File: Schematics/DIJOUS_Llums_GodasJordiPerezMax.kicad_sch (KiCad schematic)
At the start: 95 parts, among them J1 Conn_01x05_Socket, J10 Screw_Terminal_01x02, J11 Conn_01x06, J5 Conn_01x05, J6 Conn_01x03, J7 Conn_01x02, J8 DE9_Plug, J9 Conn_01x06_Socket, K1 G5LE-1 DC12, K3 G5LE-1 DC12, Q1 ZXTN19020DFFTA, Q10 ZXTN19020DFFTA, Q3 Si7336ADP, Q4 Si7336ADP, Q5 ZXTN19020DFFTA, Q6 ZXTN19020DFFTA, Q7 Si7336ADP, Q8 Si7336ADP, Q9 ZXTN19020DFFTA, U1 LT6202CS5, U2 LM2596T-ADJ, U3 PIC18F2580-I/SO, U4 MCP2551-I-SN, U5 ADP7112ACBZ-3.3-R7, U6 ADM7172ACPZ-5.0-R7, U7 PCA9306D, k2 1k

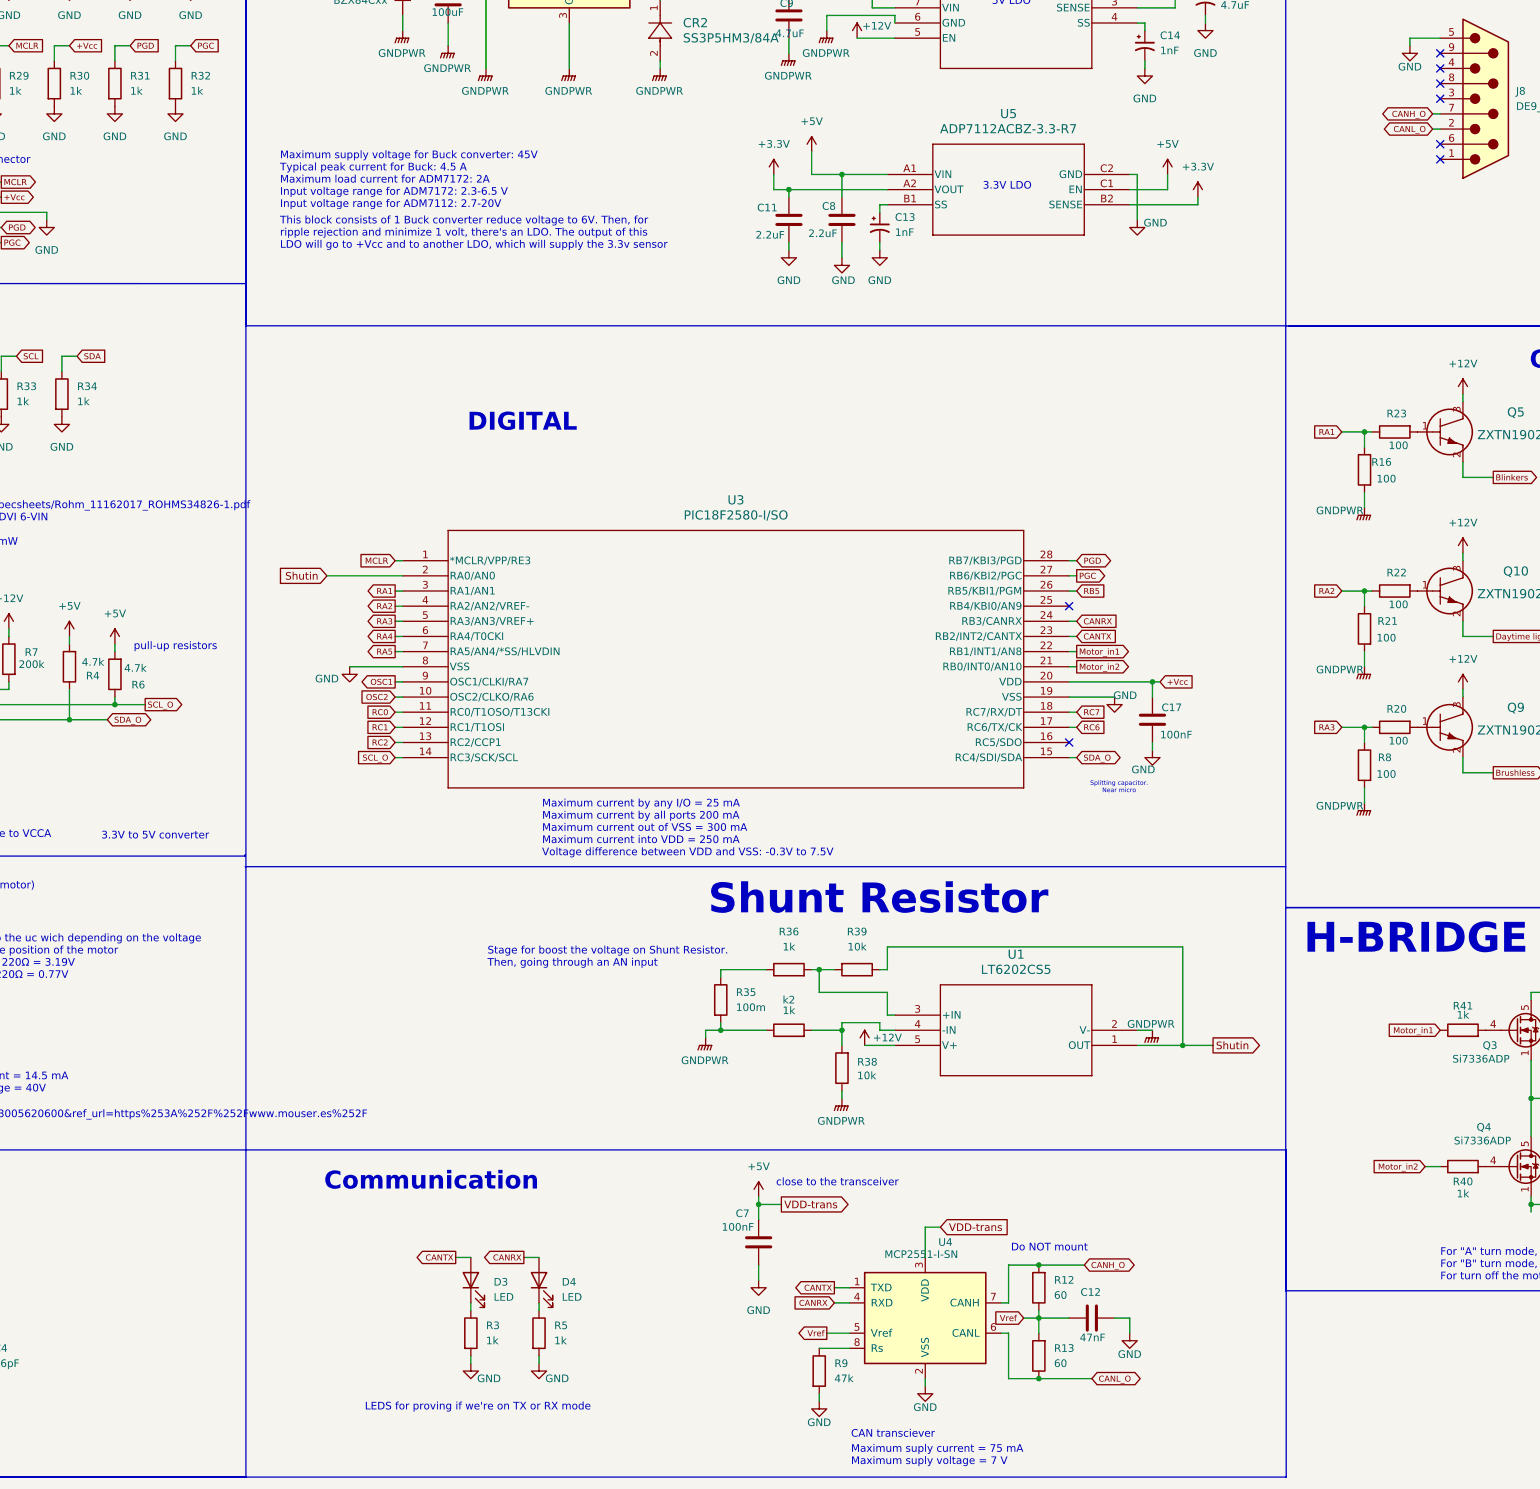
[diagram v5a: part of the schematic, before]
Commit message: Update DIJOUS_Llums_GodasJordiPerezMax.kicad_sch
Se ha cambiado alguna etiqueta
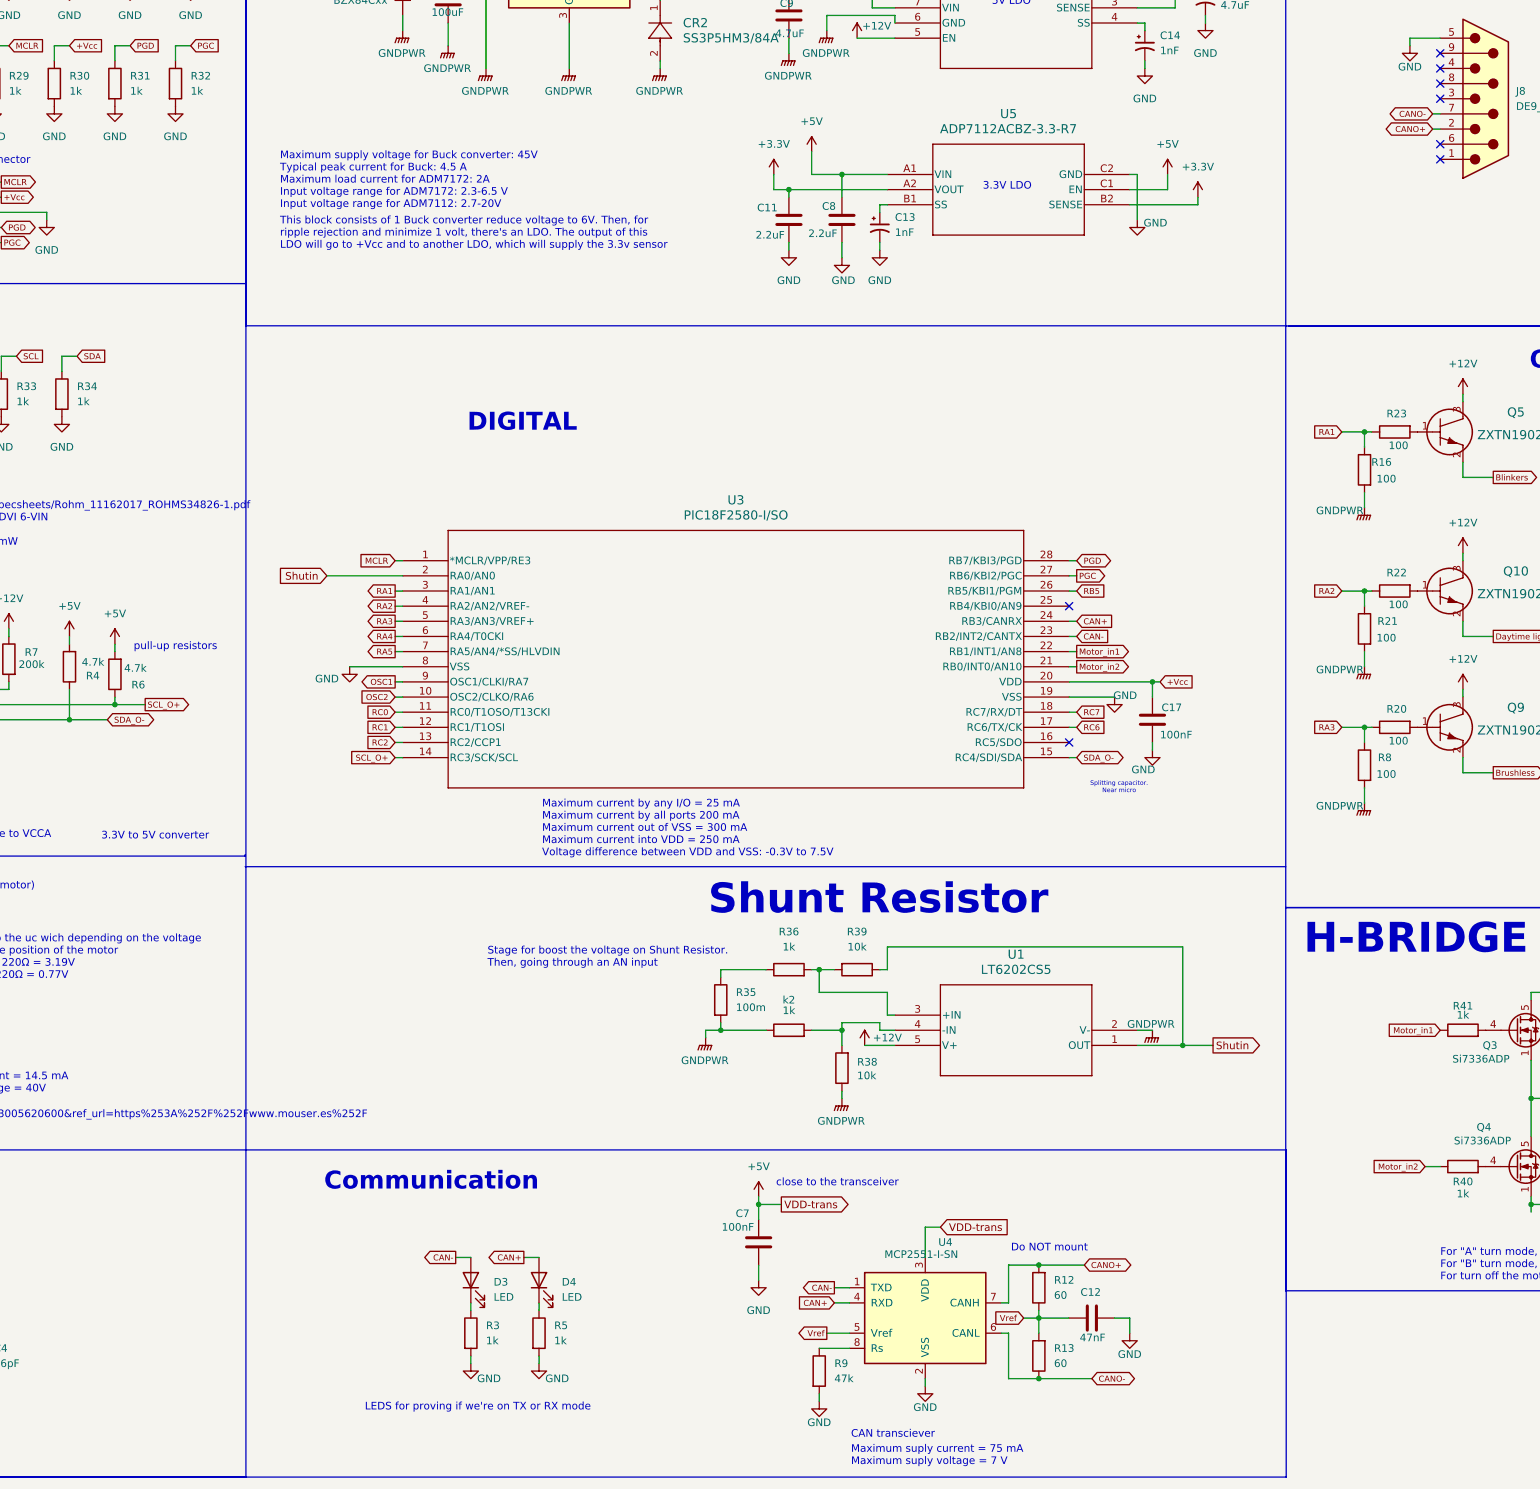
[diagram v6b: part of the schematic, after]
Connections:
- net CANH_O renamed CANO+
- net CANO+: now also J8.2; no longer J8.7
- net CANL_O renamed CANO-
- net CANO-: now also J8.7; no longer J8.2
- net CANRX renamed CAN+
- net CANTX renamed CAN-
- net SCL_O renamed SCL_O+
- net SDA_O renamed SDA_O-
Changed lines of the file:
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@@
 		)
 	)
-	(global_label "CANH_O"
+	(global_label "CANO-"
 		(shape bidirectional)
 		(at 316.23 55.88 180)
@@
 		)
 		(property "Intersheetrefs" "${INTERSHEET_REFS}"
-			(at 307.4929 55.88 0)
+			(at 307.8143 55.88 0)
 			(effects
 				(font
@@
 		)
 	)
-	(global_label "CANRX"
+	(global_label "CAN+"
 		(shape output)
 		(at 163.83 247.65 180)
@@
 		)
 		(property "Intersheetrefs" "${INTERSHEET_REFS}"
-			(at 156.6226 247.65 0)
-			(effects
-				(font
-					(size 1.27 1.27)
-				)
-				(justify right)
-				(hide yes)
-			)
-		)
-	)
-	(global_label "CANTX"
+			(at 157.3369 247.65 0)
+			(effects
+				(font
+					(size 1.27 1.27)
+				)
+				(justify right)
+				(hide yes)
+			)
+		)
+	)
+	(global_label "CAN-"
 		(shape output)
 		(at 152.4 247.65 180)
@@
 		)
 		(property "Intersheetrefs" "${INTERSHEET_REFS}"
-			(at 144.8057 247.65 0)
+			(at 145.9069 247.65 0)
 			(effects
 				(font
@@
 		)
 	)
-	(global_label "CANL_O"
+	(global_label "CANO-"
 		(shape bidirectional)
 		(at 259.08 267.97 0)
@@
 		)
 		(property "Intersheetrefs" "${INTERSHEET_REFS}"
-			(at 267.579 267.97 0)
+			(at 267.4957 267.97 0)
 			(effects
 				(font
@@
 		)
 	)
-	(global_label "CANL_O"
+	(global_label "CANO+"
 		(shape bidirectional)
 		(at 316.23 58.42 180)
@@
 		)
 		(property "Intersheetrefs" "${INTERSHEET_REFS}"
-			(at 307.731 58.42 0)
+			(at 307.8143 58.42 0)
 			(effects
 				(font
@@
 		)
 	)
-	(global_label "SDA_O"
+	(global_label "SDA_O-"
 		(shape bidirectional)
 		(at 93.98 157.48 0)
@@
 		)
 		(property "Intersheetrefs" "${INTERSHEET_REFS}"
-			(at 101.8243 157.48 0)
-			(effects
-				(font
-					(size 1.27 1.27)
-				)
-				(justify left)
-				(hide yes)
-			)
-		)
-	)
-	(global_label "CANH_O"
+			(at 103.0624 157.48 0)
+			(effects
+				(font
+					(size 1.27 1.27)
+				)
+				(justify left)
+				(hide yes)
+			)
+		)
+	)
+	(global_label "CANO+"
 		(shape bidirectional)
 		(at 257.81 248.92 0)
@@
 		)
 		(property "Intersheetrefs" "${INTERSHEET_REFS}"
-			(at 266.5471 248.92 0)
-			(effects
-				(font
-					(size 1.27 1.27)
-				)
-				(justify left)
-				(hide yes)
-			)
-		)
-	)
-	(global_label "CANRX"
+			(at 266.2257 248.92 0)
+			(effects
+				(font
+					(size 1.27 1.27)
+				)
+				(justify left)
+				(hide yes)
+			)
+		)
+	)
+	(global_label "CAN+"
 		(shape input)
 		(at 256.54 140.97 0)
@@
 		)
 		(property "Intersheetrefs" "${INTERSHEET_REFS}"
-			(at 263.7474 140.97 0)
+			(at 263.0331 140.97 0)
 			(effects
 				(font
@@
 		)
 	)
-	(global_label "SDA_O"
+	(global_label "SDA_O-"
 		(shape bidirectional)
 		(at 256.54 163.83 0)
@@
 		)
 		(property "Intersheetrefs" "${INTERSHEET_REFS}"
-			(at 263.5093 163.83 0)
+			(at 265.6224 163.83 0)
 			(effects
 				(font
@@
 		)
 	)
-	(global_label "SCL_O"
+	(global_label "SCL_O+"
 		(shape input)
 		(at 142.24 163.83 180)
@@
 		)
 		(property "Intersheetrefs" "${INTERSHEET_REFS}"
-			(at 135.3183 163.83 0)
+			(at 134.0802 163.83 0)
 			(effects
 				(font
@@
 		)
 	)
-	(global_label "SCL_O"
+	(global_label "SCL_O+"
 		(shape output)
 		(at 100.33 154.94 0)
@@
 		)
 		(property "Intersheetrefs" "${INTERSHEET_REFS}"
-			(at 107.2517 154.94 0)
+			(at 108.4898 154.94 0)
 			(effects
 				(font
@@
 		)
 	)
-	(global_label "CANTX"
+	(global_label "CAN-"
 		(shape input)
 		(at 256.54 143.51 0)
@@
 		)
 		(property "Intersheetrefs" "${INTERSHEET_REFS}"
-			(at 263.5093 143.51 0)
+			(at 263.0331 143.51 0)
 			(effects
 				(font
@@
 		)
 	)
-	(global_label "CANTX"
+	(global_label "CAN-"
 		(shape output)
 		(at 215.9 252.73 180)
@@
 		)
 		(property "Intersheetrefs" "${INTERSHEET_REFS}"
-			(at 208.3057 252.73 0)
+			(at 209.4069 252.73 0)
 			(effects
 				(font
@@
 		)
 	)
-	(global_label "CANRX"
+	(global_label "CAN+"
 		(shape input)
 		(at 215.9 255.27 180)
@@
 		)
 		(property "Intersheetrefs" "${INTERSHEET_REFS}"
-			(at 208.0676 255.27 0)
-			(effects
-				(font
+			(at 209.4069 255.27 0)
+			(effects
+				(font

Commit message: Update DIJOUS_Llums_GodasJordiPerezMax.kicad_sch
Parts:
- removed F1: Fuse, symbol Device:Fuse
- removed U1: LT6202CS5, S_5_ADI, symbol LT6202CS5:LT6202CS5
- added C16: 100nF, Capacitor_SMD:C_1206_3216Metric_Pad1.33x1.80mm_HandSolder, symbol Device:C
- added R37, R39, R43, R44: 10k, Resistor_SMD:R_0402_1005Metric, symbol Device:R
- added U7: LT6202CS5, LT6202CS5:S_5_ADI, symbol LT6202CS5:LT6202CS5
- renumbered C3 to C1, C8 to C10, C13 to C11, C14 to C13, C17 to C14, C16 to C15, C1 to C2, C15 to C3, C2 to C4, C4 to C5, C9 to C8, C11 to C9, CR2 to CR1, D5 to D1, D6 to D2, D9 to D5, D1 to D6, D2 to D7, D7 to D8, J6 to J1, J11 to J2, J10 to J3, J1 to J4, J8 to J6, J9 to J8, K3 to K2, Q5 to Q1, Q10 to Q2, Q9 to Q3, Q3 to Q4, Q4 to Q5, Q1 to Q7, Q7 to Q8, Q8 to Q9, R34 to R10, R26 to R11, R4 to R12, R31 to R13, R6 to R14, R27 to R15, R32 to R16, R28 to R17, R3 to R18, R5 to R19, R14 to R2, R9 to R20, R10 to R21, R11 to R22, R12 to R23, R13 to R24, R15 to R25, R16 to R26, R21 to R27, R8 to R28, R35 to R29, R2 to R3, R23 to R30, R22 to R31, R20 to R32, R36 to R33, k2 to R34, R41 to R35, R40 to R36, R24 to R4, R39 to R40, R19 to R41, R37 to R42, R42 to R45, R43 to R46, R29 to R5, R33 to R6, R25 to R7, R7 to R8, R30 to R9, U7 to U1, U3 to U2, U2 to U3
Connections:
- net Shunt_in is gone; now on net Shutin: D6.2 (A), D7.2 (A), Q5.1 (S), Q5.2 (S), Q5.3 (S), Q9.1 (S), Q9.2 (S), Q9.3 (S)
- net fuse_node is gone; now on net +12V: J3.2 (Pin_2)
- net +12V: no longer R8.1
- net +5V: now also R8.1, C16.1, U7.5 (V+)
- net GND: now also R26.2, R27.2, R28.2, R29.2, R34.1, R38.1, R41.2, R42.2, C16.2, R37.2, R39.2, R43.2, R44.2, U7.2 (V-)
- net GNDPWR: no longer R26.2, R27.2, R28.2, R29.2, R34.1, R38.1, R41.2, R42.2
- net Shutin: now also U7.1 (OUT)
- net at Q8.4 (G), R45.1: now also R43.1
- net at R34.2, R38.2: now also U7.4 (-IN)
- net at R33.2, R40.2: now also U7.3 (+IN)
- net at Q9.4 (G), R46.1: now also R44.1
- net at Q4.4 (G), R35.2: now also R37.1
- net at Q5.4 (G), R36.2: now also R39.1
- net CAN+ renamed CANRX
- net CAN- renamed CANTX
- net CANO+ renamed CANH_O
- net CANH_O: now also J6.7; no longer J6.2
- net CANO- renamed CANL_O
- net CANL_O: now also J6.2; no longer J6.7
- net SCL_O+ renamed SCL_O
- net SDA_O- renamed SDA_O
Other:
- note added: "Spliting capacity, near the LT6202CS5"
- note added: "Splitting capacitors, 2 Near VREF1 and VREF2"
- note removed: "Shunt Resistor"
- note removed: "Splitting capacitor. 2 Near VREF1 and VREF2"
- moved on the sheet: C12, C7, C8, D3, D4, D5, D6, D7, D8, J3, J6, J7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
